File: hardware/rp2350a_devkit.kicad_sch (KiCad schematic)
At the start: 55 parts, among them J1 USB_C_Receptacle_USB2.0_16P, J2 Conn_01x03, J3 Conn_01x16, J4 Conn_01x16, SW1 SW_Push, SW2 SW_Push, U1 NCP1117-3.3_SOT223, U2 USBLC6-2SC6, U3 W25Q128JVS, Y1 Crystal_GND24

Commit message: add images and files for v1.0a
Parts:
- removed R11: 1k, Resistor_SMD:R_0402_1005Metric, symbol Device:R
- removed U1: NCP1117-3.3_SOT223, Package_TO_SOT_SMD:SOT-223-3_TabPin2, symbol Regulator_Linear:NCP1117-3.3_SOT223
- added D1: D_Schottky, Diode_SMD:D_SOD-123, symbol Device:D_Schottky
- added R8: 10k, Resistor_SMD:R_0603_1608Metric, symbol Device:R
- added U1: AP2112K-3.3, Package_TO_SOT_SMD:SOT-23-5, symbol Regulator_Linear:AP2112K-3.3
- C10: renamed from C3; footprint Capacitor_SMD:C_0402_1005Metric -> Capacitor_SMD:C_0603_1608Metric
- C11: renamed from C6; value 100u -> 100n; footprint Capacitor_SMD:C_0402_1005Metric -> Capacitor_SMD:C_0603_1608Metric
- C12: renamed from C7; footprint Capacitor_SMD:C_0402_1005Metric -> Capacitor_SMD:C_0603_1608Metric
- C13: renamed from C8; footprint Capacitor_SMD:C_0402_1005Metric -> Capacitor_SMD:C_0603_1608Metric
- C14: renamed from C9; footprint Capacitor_SMD:C_0603_1608Metric -> Capacitor_SMD:C_0805_2012Metric
- C15: renamed from C10; footprint Capacitor_SMD:C_0402_1005Metric -> Capacitor_SMD:C_0603_1608Metric
- C16: renamed from C11; footprint Capacitor_SMD:C_0402_1005Metric -> Capacitor_SMD:C_0603_1608Metric
- C17: renamed from C12; footprint Capacitor_SMD:C_0402_1005Metric -> Capacitor_SMD:C_0603_1608Metric
- C18: renamed from C13; footprint Capacitor_SMD:C_0402_1005Metric -> Capacitor_SMD:C_0603_1608Metric
- C19: renamed from C14; footprint Capacitor_SMD:C_0402_1005Metric -> Capacitor_SMD:C_0603_1608Metric
- C20: renamed from C15; footprint Capacitor_SMD:C_0402_1005Metric -> Capacitor_SMD:C_0603_1608Metric
- C21: renamed from C16; footprint Capacitor_SMD:C_0402_1005Metric -> Capacitor_SMD:C_0603_1608Metric
- C22: renamed from C17; footprint Capacitor_SMD:C_0402_1005Metric -> Capacitor_SMD:C_0603_1608Metric
- C23: renamed from C18; footprint Capacitor_SMD:C_0402_1005Metric -> Capacitor_SMD:C_0603_1608Metric
- C24: renamed from C19; footprint Capacitor_SMD:C_0603_1608Metric -> Capacitor_SMD:C_0805_2012Metric
- C3: renamed from C4; footprint Capacitor_SMD:C_0402_1005Metric -> Capacitor_SMD:C_0603_1608Metric
- C4: renamed from C5; footprint Capacitor_SMD:C_0402_1005Metric -> Capacitor_SMD:C_0603_1608Metric
- C5: renamed from C20; footprint Capacitor_SMD:C_0402_1005Metric -> Capacitor_SMD:C_0603_1608Metric
- C6: renamed from C21; footprint footprints:C_0402_smallpads -> Capacitor_SMD:C_0603_1608Metric
- C7: renamed from C22; footprint footprints:C_0402_smallpads -> Capacitor_SMD:C_0603_1608Metric
- C8: renamed from C23; footprint Capacitor_SMD:C_0402_1005Metric -> Capacitor_SMD:C_0603_1608Metric
- C9: renamed from C24; footprint Capacitor_SMD:C_0603_1608Metric -> Capacitor_SMD:C_0805_2012Metric
- D2: renamed from D1; footprint LED_SMD:LED_0402_1005Metric -> LED_SMD:LED_0603_1608Metric
- D3: renamed from D2; footprint LED_SMD:LED_0402_1005Metric -> LED_SMD:LED_0603_1608Metric
- J2: renamed from J1; LCSC PN (none) -> C2988369; MNF PART # C2988369 -> (none)
- L1: LCSC PN (none) -> C42411119; MNF PART # C42411119 -> (none)
- R1: footprint Resistor_SMD:R_0402_1005Metric -> Resistor_SMD:R_0603_1608Metric
- R10: renamed from R12; footprint Resistor_SMD:R_0402_1005Metric -> Resistor_SMD:R_0603_1608Metric
- R11: renamed from R2; footprint Resistor_SMD:R_0402_1005Metric -> Resistor_SMD:R_0603_1608Metric
- R12: renamed from R3; footprint Resistor_SMD:R_0402_1005Metric -> Resistor_SMD:R_0603_1608Metric
- R13: renamed from R6; footprint Resistor_SMD:R_0402_1005Metric -> Resistor_SMD:R_0603_1608Metric
- R2: renamed from R5; footprint Resistor_SMD:R_0402_1005Metric -> Resistor_SMD:R_0603_1608Metric
- R3: renamed from R4; footprint Resistor_SMD:R_0402_1005Metric -> Resistor_SMD:R_0603_1608Metric
- R4: renamed from R9; footprint Resistor_SMD:R_0402_1005Metric -> Resistor_SMD:R_0603_1608Metric
- R5: renamed from R10; footprint Resistor_SMD:R_0402_1005Metric -> Resistor_SMD:R_0603_1608Metric
- R6: renamed from R7; footprint Resistor_SMD:R_0402_1005Metric -> Resistor_SMD:R_0603_1608Metric
- R7: renamed from R8; footprint Resistor_SMD:R_0402_1005Metric -> Resistor_SMD:R_0603_1608Metric
- R9: renamed from R13; footprint Resistor_SMD:R_0402_1005Metric -> Resistor_SMD:R_0603_1608Metric
- U2: renamed from U4; value ~ -> RP2350A; LCSC PN (none) -> C42411118
- U3: LCSC PN (none) -> C113767
- U4: renamed from U2; PCSC PN (none) -> C7519
- Y1: LCSC PN (none) -> C20625731; MNF PART # C20625731 -> (none)
- renumbered J2 to J1, SW2 to SW1, SW1 to SW2
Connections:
- net +3V3: now also R8.2, U1.5 (VOUT)
- net GND: now also J1.2 (Pin_2), J4.16 (Pin_16), U1.2 (GND); no longer J1.3 (Pin_3), J4.1 (Pin_1)
- net RUN_SW: now also U2.26 (RUN), R8.1
- net SWCLK: now also J1.3 (Pin_3); no longer J1.1 (Pin_1)
- net SWD: now also J1.1 (Pin_1); no longer J1.2 (Pin_2)
- net VBUS: now also J4.1 (Pin_1), D1.2 (A); no longer C1.1
- net POWER_LED: now reaches D2.1 (K), R3.1
- new net 5VIN: C1.1, D1.1 (K), U1.1 (VIN), U1.3 (EN)
- no-connect marks 3 -> 2
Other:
- note added: "10u selected over 1u as it is used elsewhere"
- note added: "See RP2350 hardware design Footprints and layout deviate from the reccomendation."
- note added: "USB 2.0"
- note added: "Voltage Regulator + indicator LED"
- note added: "changed ldo, added schottky added pull-up to run sw changed footprint to 0603 0804 instead of 0402 0603 added vbus to gpio"
- note removed: "C and R must be 0402, 1005 metric L must be AOTA-B201610S3R3-101-T (0806, 2016 metric) See RP2350 hardware design"
- note removed: "C1 C2 Should be ceramic or tantalum cap"
- note removed: "USB + Power"
- moved on the sheet: C1, C10, C11, C12, C13, C14, C15, C16, C17, C18, C19, C2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

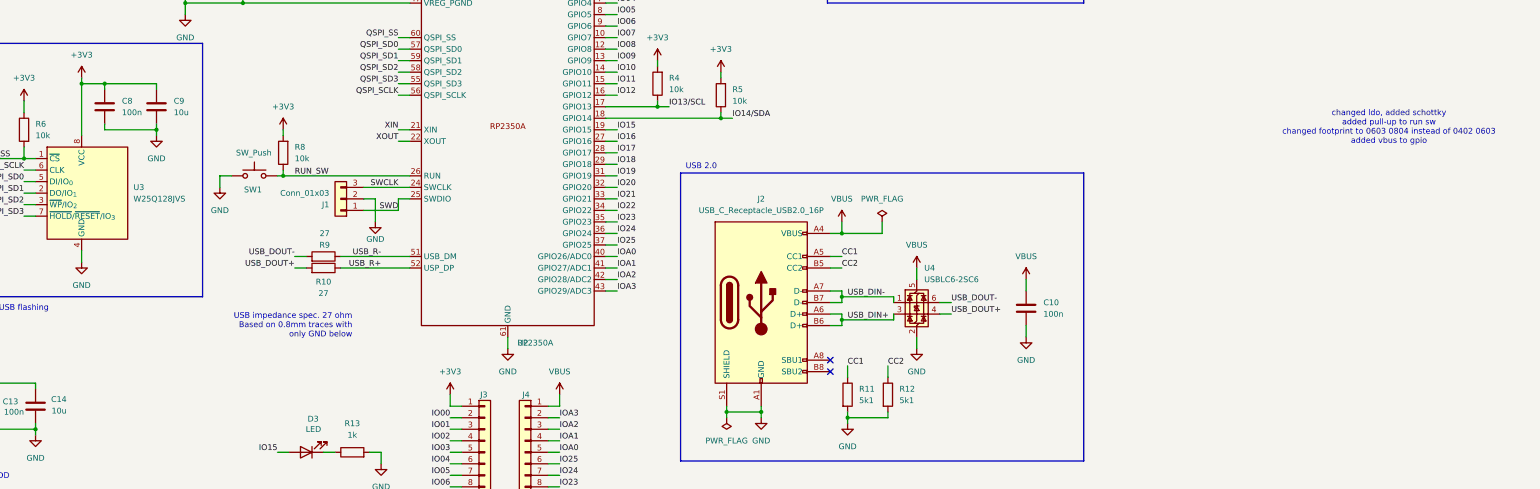
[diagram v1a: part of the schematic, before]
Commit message: re-routed pcb for a better ground plane
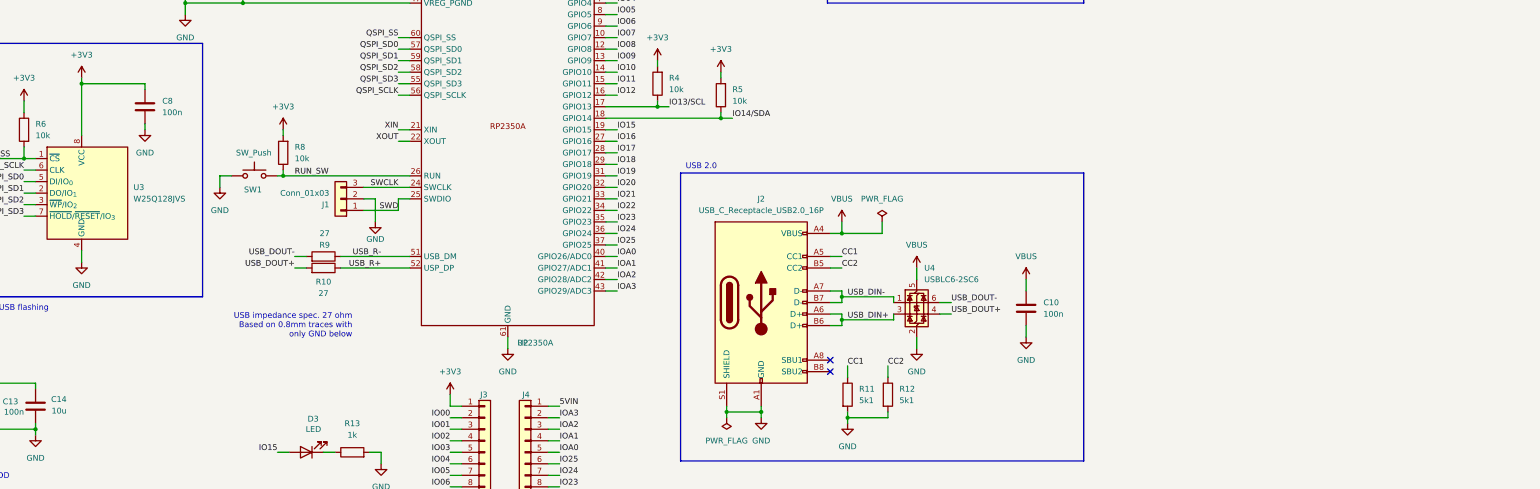
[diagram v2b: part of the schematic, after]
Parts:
- removed C9: 10u, Capacitor_SMD:C_0805_2012Metric, symbol Device:C
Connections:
- net 5VIN: now also J4.1 (Pin_1)
- net VBUS: no longer J4.1 (Pin_1)
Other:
- note removed: "changed ldo, added schottky added pull-up to run sw changed footprint to 0603 0804 instead of 0402 0603 added vbus to gpio"
- moved on the sheet: C8

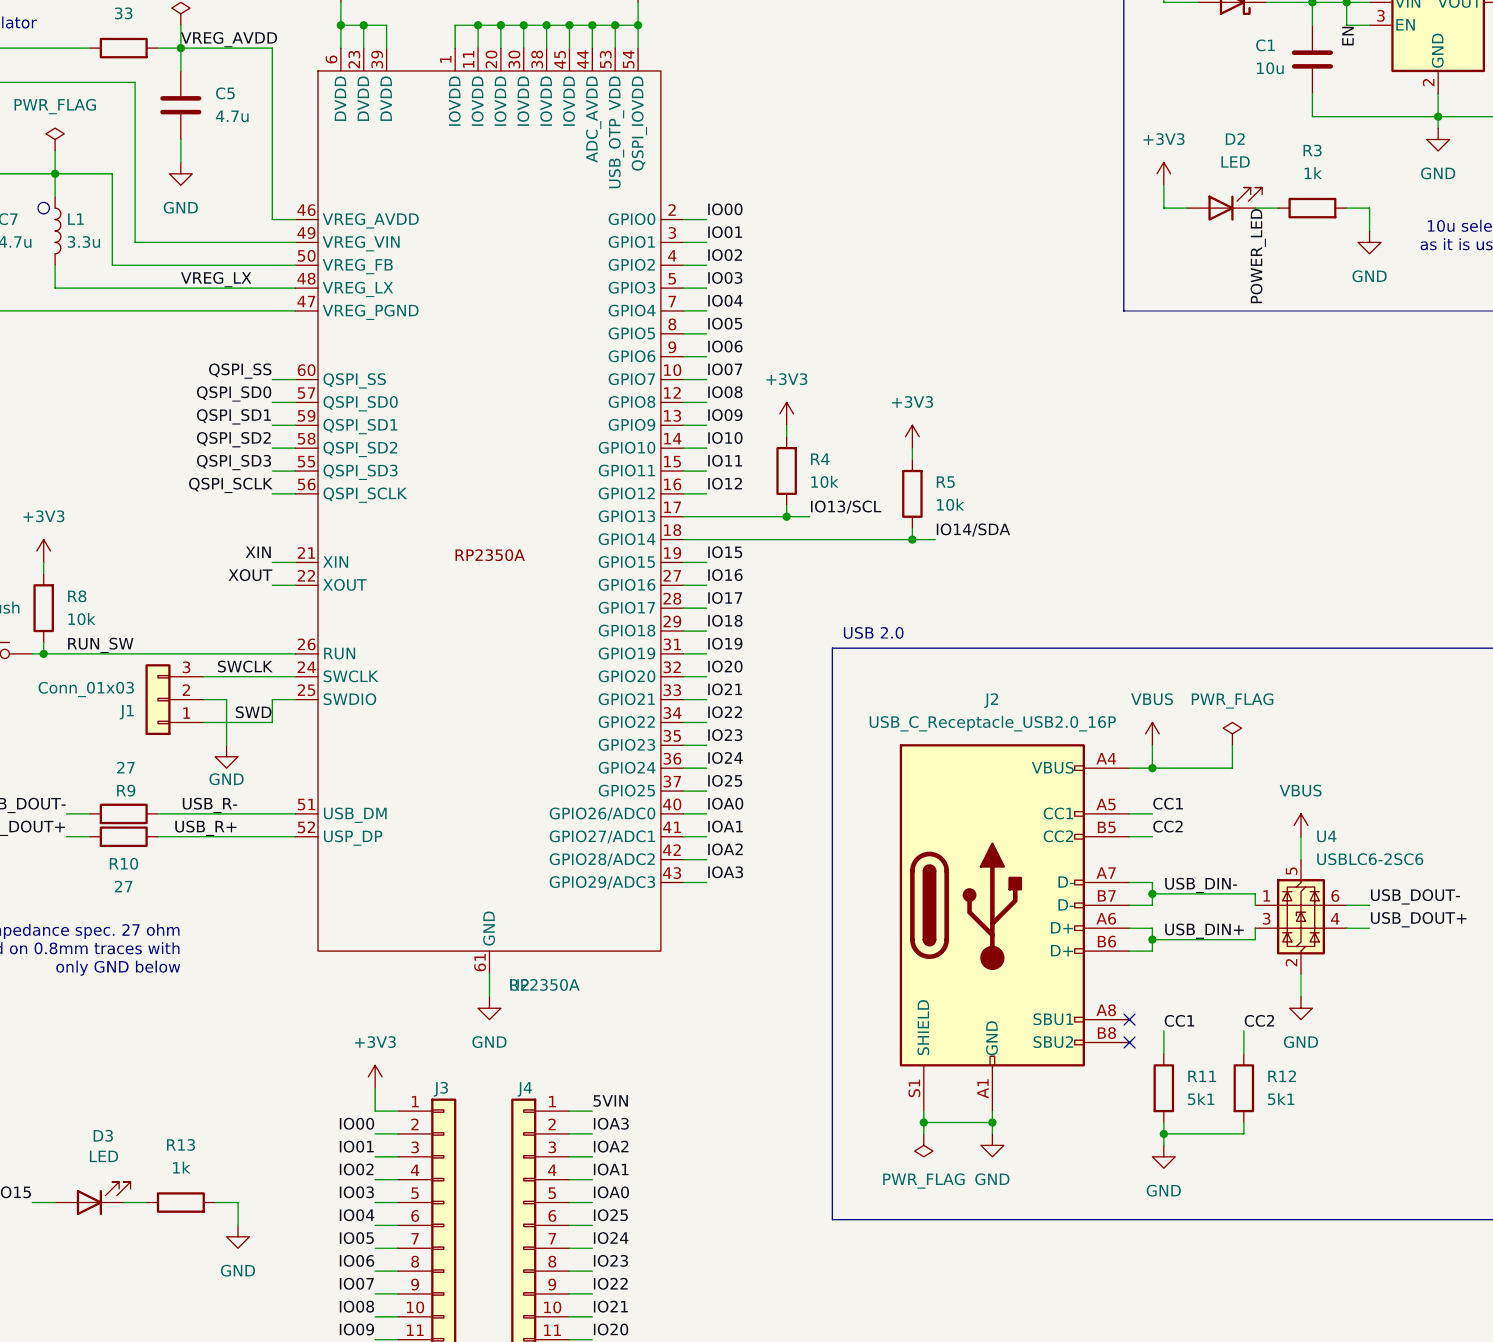
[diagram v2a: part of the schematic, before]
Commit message: update 3d pcb image, fix silkscreen placement and resistor values
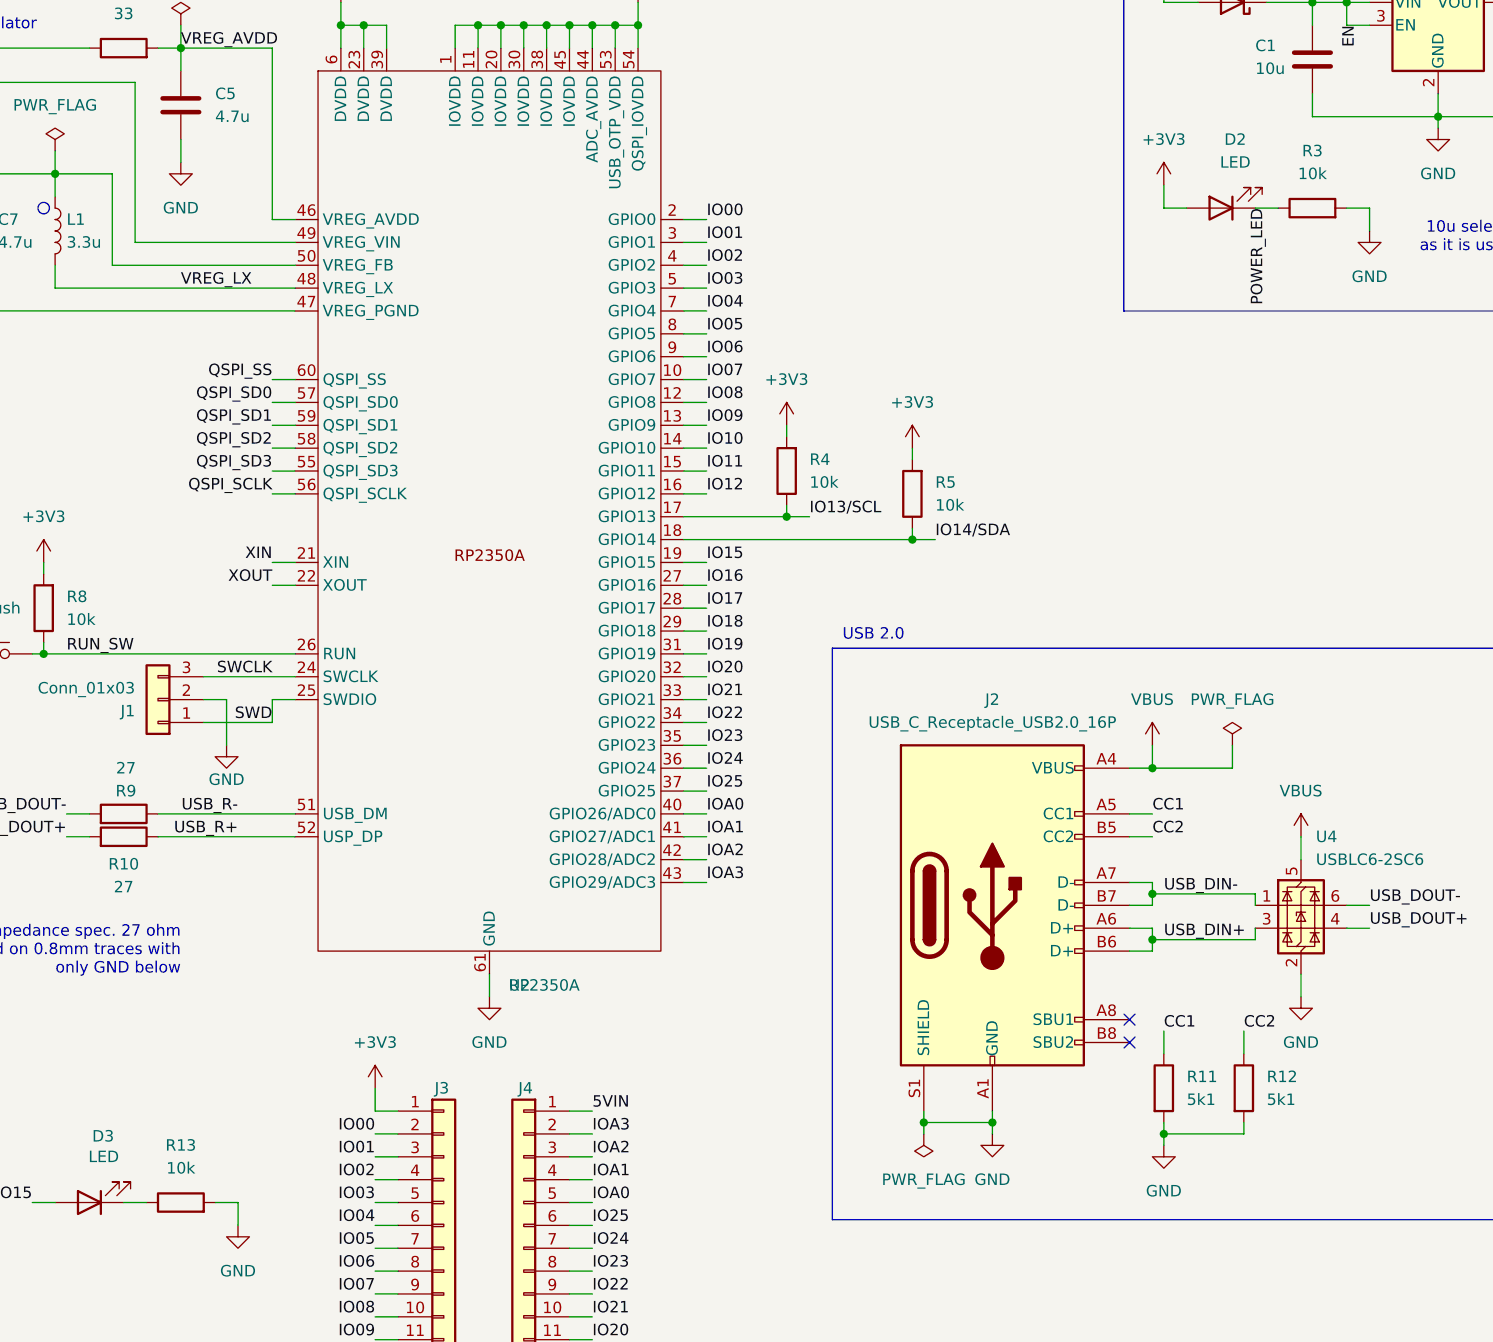
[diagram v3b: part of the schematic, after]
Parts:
- R13, R3: value 1k -> 10k
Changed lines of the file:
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@@
 			)
 		)
-		(property "Value" "1k"
+		(property "Value" "10k"
 			(at 246.38 46.99 90)
 			(effects
@@
 			)
 		)
-		(property "Value" "1k"
+		(property "Value" "10k"
 			(at 120.65 157.48 90)
 			(effects

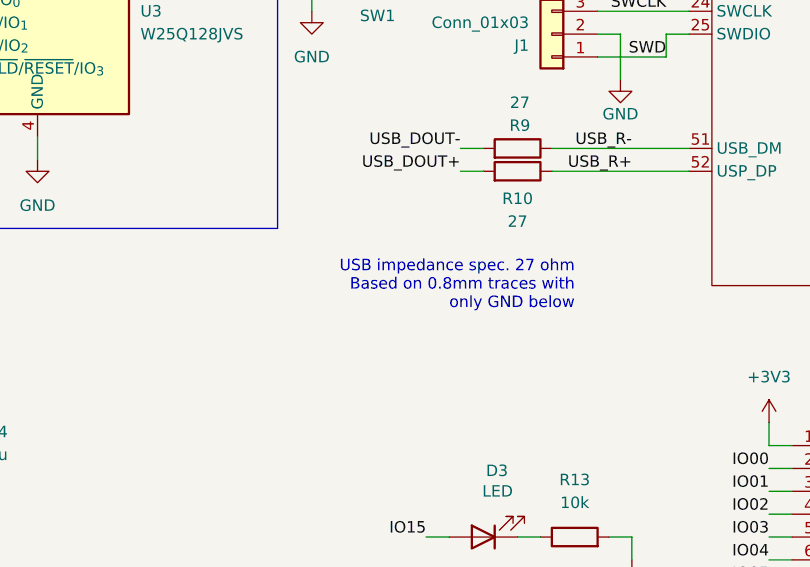
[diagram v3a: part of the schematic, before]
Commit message: changed button footprint
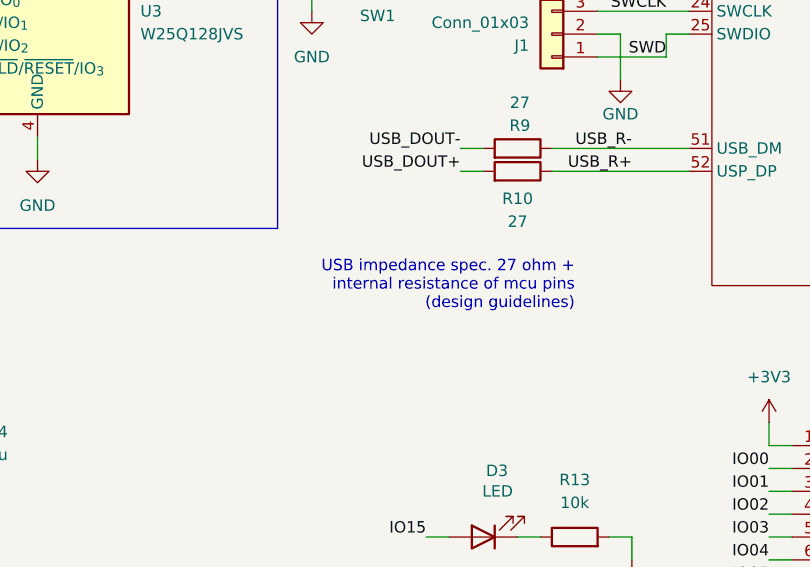
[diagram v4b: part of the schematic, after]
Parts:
- SW1, SW2: footprint Button_Switch_SMD:SW_SPST_B3U-1000P -> footprints:TS-1088-AR02016; LCSC PN (none) -> C720477
- U4: LCSC PN (none) -> C7519; PCSC PN C7519 -> (none)
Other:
- note added: "USB impedance spec. 27 ohm + internal resistance of mcu pins (design guidelines)"
- note removed: "USB impedance spec. 27 ohm Based on 0.8mm traces with only GND below"
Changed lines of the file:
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@@
 		)
 	)
-	(text "USB impedance spec. 27 ohm\nBased on 0.8mm traces with \nonly GND below"
+	(text "USB impedance spec. 27 ohm +\ninternal resistance of mcu pins\n(design guidelines)"
 		(exclude_from_sim no)
 		(at 120.65 133.35 0)
@@
 			)
 		)
-		(property "Footprint" "Button_Switch_SMD:SW_SPST_B3U-1000P"
+		(property "Footprint" "footprints:TS-1088-AR02016"
 			(at 99.06 95.25 0)
 			(effects
@@
 			)
 		)
+		(property "LCSC PN" "C720477"
+			(at 99.06 100.33 0)
+			(effects
+				(font
+					(size 1.27 1.27)
+				)
+				(hide yes)
+			)
+		)
 		(pin "1"
 		)
@@
 			)
 		)
-		(property "Footprint" "Button_Switch_SMD:SW_SPST_B3U-1000P"
+		(property "Footprint" "footprints:TS-1088-AR02016"
 			(at 17.78 104.14 0)
 			(effects
@@
 			)
 		)
+		(property "LCSC PN" "C720477"
+			(at 22.86 104.14 90)
+			(effects
+				(font
+					(size 1.27 1.27)
+				)
+				(hide yes)
+			)
+		)
 		(pin "1"
 		)
@@
 			)
 		)
-		(property "PCSC PN" "C7519"
+		(property "LCSC PN" "C7519"
 			(at 245.11 128.27 0)
 			(effects
